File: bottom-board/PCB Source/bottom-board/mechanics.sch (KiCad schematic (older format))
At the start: 6 parts

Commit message: rev 0.0.3
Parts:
- added H1: HOLE, Uno:Hole_3.5mm, symbol bottom-board-rescue:HOLE-local-components
- added H6, H7: MountingHole_Pad, MountingHole:MountingHole_3.2mm_M3_DIN965_Pad, symbol bottom-board-rescue:MountingHole_Pad-Mechanical
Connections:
- no-connect marks 0 -> 2
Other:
- note added: "SOM Mounting holes"
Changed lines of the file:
@@
 	1    0    0    -1
 $EndComp
+$Comp
+L bottom-board-rescue:HOLE-local-components H?
+U 1 1 5F8174D3
+P 2500 2240
+AR Path="/5F8174D3" Ref="H?"  Part="1"
+AR Path="/55FC02AF/5F8174D3" Ref="H1"  Part="1"
+F 0 "H1" H 2500 2060 50  0000 C CNN
+F 1 "HOLE" H 2500 2410 50  0000 C CNN
+F 2 "Uno:Hole_3.5mm" H 2500 2240 60  0001 C CNN
+F 3 "" H 2500 2240 60  0000 C CNN
+	1    2500 2240
+	1    0    0    -1
+$EndComp
+$Comp
+L bottom-board-rescue:MountingHole_Pad-Mechanical H?
+U 1 1 5F81B775
+P 1440 3015
+AR Path="/54F7244B/5F81B775" Ref="H?"  Part="1"
+AR Path="/55FC02AF/5F81B775" Ref="H6"  Part="1"
+F 0 "H6" H 1540 3064 50  0000 L CNN
+F 1 "MountingHole_Pad" H 1540 2973 50  0000 L CNN
+F 2 "MountingHole:MountingHole_3.2mm_M3_DIN965_Pad" H 1440 3015 50  0001 C CNN
+F 3 "~" H 1440 3015 50  0001 C CNN
+	1    1440 3015
+	1    0    0    -1
+$EndComp
+$Comp
+L bottom-board-rescue:MountingHole_Pad-Mechanical H?
+U 1 1 5F81B998
+P 2320 2990
+AR Path="/54F7244B/5F81B998" Ref="H?"  Part="1"
+AR Path="/55FC02AF/5F81B998" Ref="H7"  Part="1"
+F 0 "H7" H 2420 3039 50  0000 L CNN
+F 1 "MountingHole_Pad" H 2420 2948 50  0000 L CNN
+F 2 "MountingHole:MountingHole_3.2mm_M3_DIN965_Pad" H 2320 2990 50  0001 C CNN
+F 3 "~" H 2320 2990 50  0001 C CNN
+	1    2320 2990
+	1    0    0    -1
+$EndComp
+NoConn ~ 1440 3115
+NoConn ~ 2320 3090
+Text Notes 1510 3265 0    60   ~ 0
+SOM Mounting holes
 $EndSCHEMATC

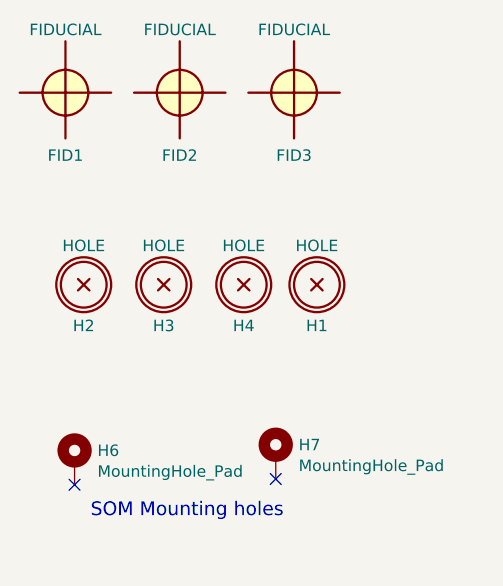
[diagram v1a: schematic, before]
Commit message: change design to 4 layer PCB
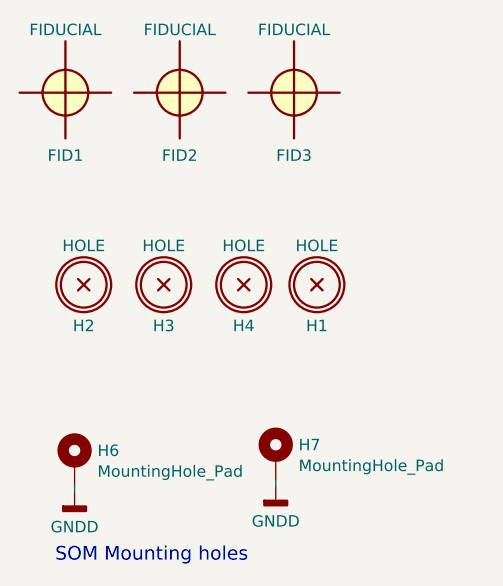
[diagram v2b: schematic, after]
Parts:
- H6, H7: MPN (none) -> 9774027151R
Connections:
- net GNDD: now reaches H6.1
- net GNDD: now also H7.1
- no-connect marks 2 -> 0
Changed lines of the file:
@@
 F 2 "MountingHole:MountingHole_3.2mm_M3_DIN965_Pad" H 1440 3015 50  0001 C CNN
 F 3 "~" H 1440 3015 50  0001 C CNN
+F 4 "9774027151R" H 1440 3015 50  0001 C CNN "MPN"
 	1    1440 3015
 	1    0    0    -1
@@
 F 2 "MountingHole:MountingHole_3.2mm_M3_DIN965_Pad" H 2320 2990 50  0001 C CNN
 F 3 "~" H 2320 2990 50  0001 C CNN
+F 4 "9774027151R" H 2320 2990 50  0001 C CNN "MPN"
 	1    2320 2990
 	1    0    0    -1
 $EndComp
-NoConn ~ 1440 3115
-NoConn ~ 2320 3090
-Text Notes 1510 3265 0    60   ~ 0
+Text Notes 1355 3460 0    60   ~ 0
 SOM Mounting holes
+$Comp
+L bottom-board-rescue:GNDD-power #PWR?
+U 1 1 5FE7AA08
+P 1440 3150
+AR Path="/54F72FB8/5FE7AA08" Ref="#PWR?"  Part="1"
+AR Path="/54F7244B/5FE7AA08" Ref="#PWR?"  Part="1"
+AR Path="/55FC02AF/5FE7AA08" Ref="#PWR0287"  Part="1"
+F 0 "#PWR0287" H 1440 2900 50  0001 C CNN
+F 1 "GNDD" H 1440 3000 50  0000 C CNN
+F 2 "" H 1440 3150 60  0000 C CNN
+F 3 "" H 1440 3150 60  0000 C CNN
+	1    1440 3150
+	1    0    0    -1
+$EndComp
+$Comp
+L bottom-board-rescue:GNDD-power #PWR?
+U 1 1 5FE7B9AF
+P 2320 3125
+AR Path="/54F72FB8/5FE7B9AF" Ref="#PWR?"  Part="1"
+AR Path="/54F7244B/5FE7B9AF" Ref="#PWR?"  Part="1"
+AR Path="/55FC02AF/5FE7B9AF" Ref="#PWR0288"  Part="1"
+F 0 "#PWR0288" H 2320 2875 50  0001 C CNN
+F 1 "GNDD" H 2320 2975 50  0000 C CNN
+F 2 "" H 2320 3125 60  0000 C CNN
+F 3 "" H 2320 3125 60  0000 C CNN
+	1    2320 3125
+	1    0    0    -1
+$EndComp
+Wire Wire Line
+	2320 3090 2320 3125
+Wire Wire Line
+	1440 3150 1440 3115
 $EndSCHEMATC

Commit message: cleanup BOM lines
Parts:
- H6, H7: MPN 9774027151R -> 9774030243R
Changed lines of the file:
@@
 encoding utf-8
 Sheet 10 11
-Title "MOD Uno - Main Board"
-Date "2019-08-16"
-Rev "0.1"
+Title "MOD Dwarf - Main Board"
+Date "2021-04-07"
+Rev "1.2"
 Comp "MOD Devices GmbH"
-Comment1 "Uno Audio processing board"
-Comment2 "https://github.com/moddevices/hw-mod-uno"
+Comment1 "Dwarf Audio processing board"
+Comment2 "https://github.com/moddevices/hw-mod-dwarf"
 Comment3 "Inp Power: 12V 500mA"
 Comment4 "USB outp Power: 500mA"
@@
 F 2 "MountingHole:MountingHole_3.2mm_M3_DIN965_Pad" H 1440 3015 50  0001 C CNN
 F 3 "~" H 1440 3015 50  0001 C CNN
-F 4 "9774027151R" H 1440 3015 50  0001 C CNN "MPN"
+F 4 "9774030243R" H 1440 3015 50  0001 C CNN "MPN"
 	1    1440 3015
 	1    0    0    -1
@@
 F 2 "MountingHole:MountingHole_3.2mm_M3_DIN965_Pad" H 2320 2990 50  0001 C CNN
 F 3 "~" H 2320 2990 50  0001 C CNN
-F 4 "9774027151R" H 2320 2990 50  0001 C CNN "MPN"
+F 4 "9774030243R" H 2320 2990 50  0001 C CNN "MPN"
 	1    2320 2990
 	1    0    0    -1
